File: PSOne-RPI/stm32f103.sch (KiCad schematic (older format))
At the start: 13 parts, among them J10 Controller-Port, J11 Controller-Port, SW1 PWR_BTN, SW2 CD_CLOSED, U7 STM32F103RBTx, Y1 8MHz

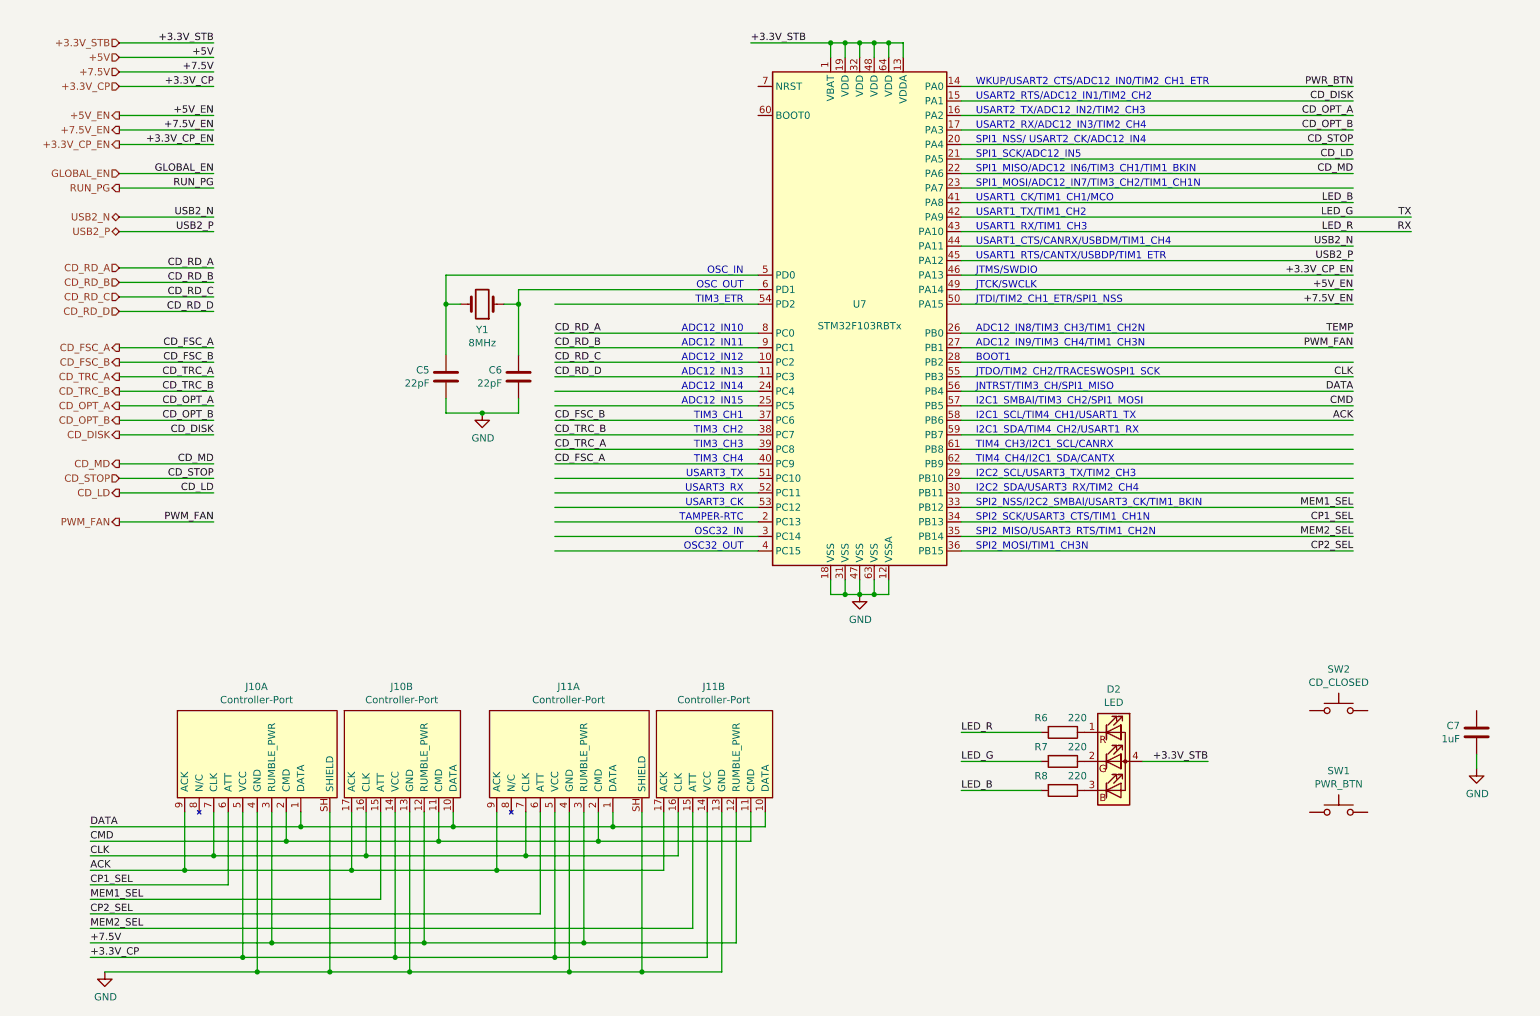
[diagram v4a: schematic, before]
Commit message: Added possibility to use the STM32 as RTC
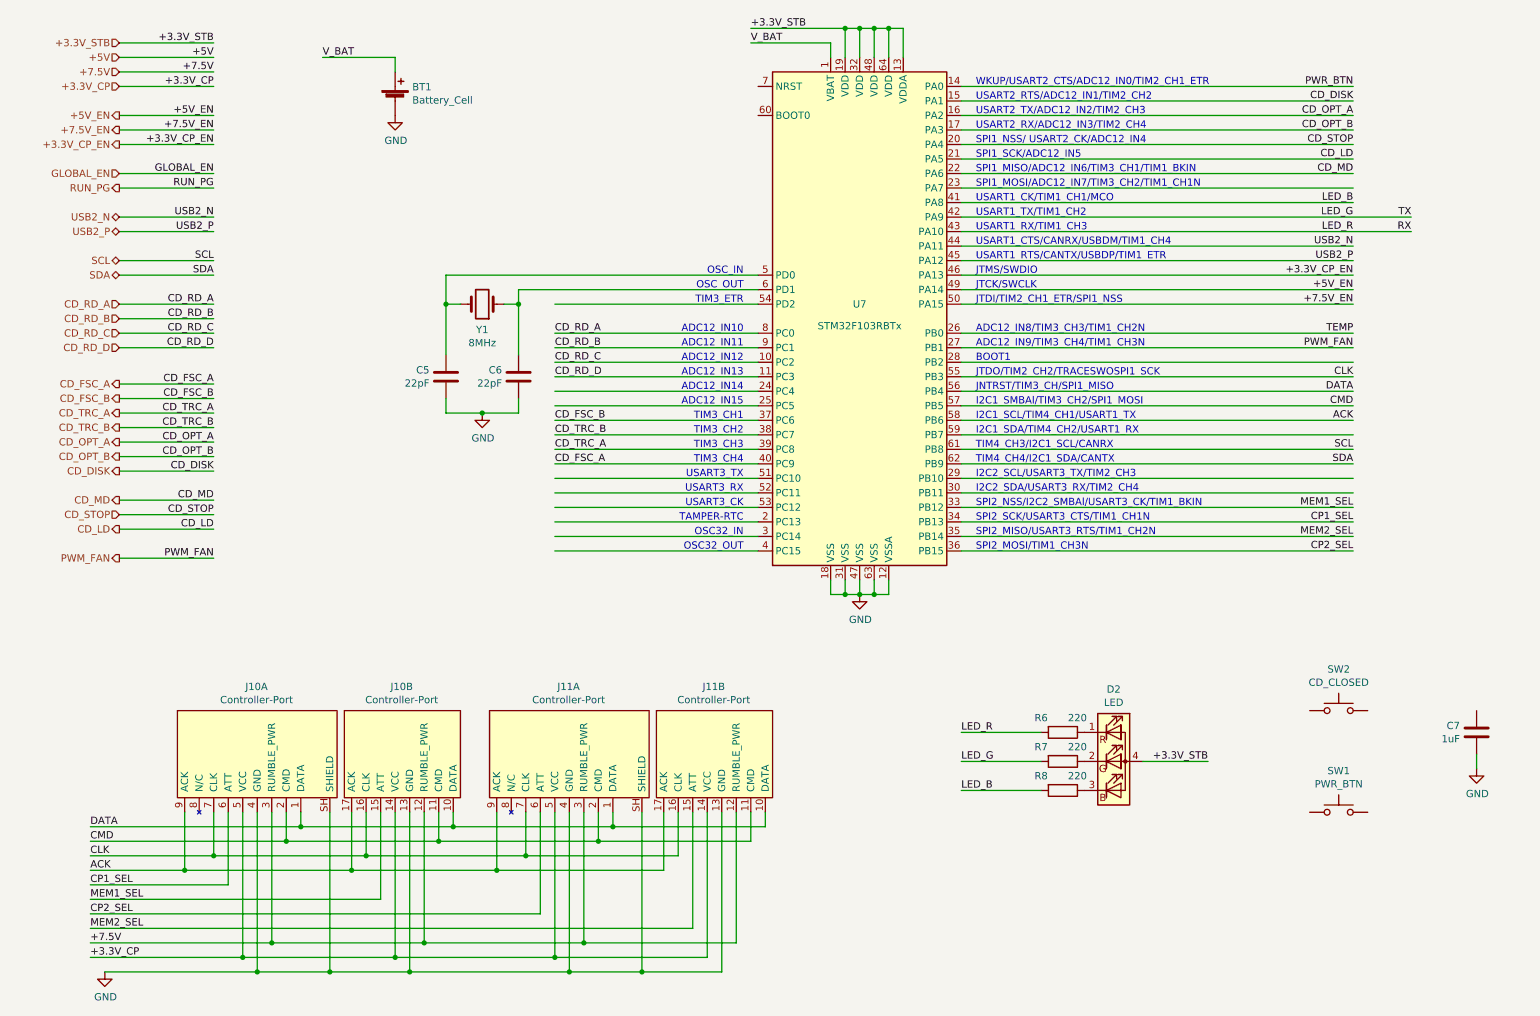
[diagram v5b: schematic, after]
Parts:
- added BT1: Battery_Cell, Battery:BatteryHolder_Keystone_1058_1x2032, symbol Device:Battery_Cell
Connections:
- net labels added: SCL, SDA, V_BAT
- wire segments 181 -> 185
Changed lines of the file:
@@
 Text Label 1200 6250 0    50   ~ 0
 DATA
-Wire Wire Line
-	6300 850  6400 850
-Wire Wire Line
-	6700 850  6700 950
-Wire Wire Line
-	6300 850  6300 950
-Wire Wire Line
-	6600 950  6600 850
-Connection ~ 6600 850
-Wire Wire Line
-	6600 850  6700 850
-Wire Wire Line
-	6500 950  6500 850
-Connection ~ 6500 850
-Wire Wire Line
-	6500 850  6600 850
-Wire Wire Line
-	6400 950  6400 850
-Connection ~ 6400 850
-Wire Wire Line
-	6400 850  6500 850
-Connection ~ 6300 850
-Text Label 5750 850  0    50   ~ 0
+Connection ~ 6600 750
+Wire Wire Line
+	6600 750  6700 750
+Connection ~ 6500 750
+Wire Wire Line
+	6500 750  6600 750
+Connection ~ 6400 750
+Wire Wire Line
+	6400 750  6500 750
+Text Label 5750 750  0    50   ~ 0
 +3.3V_STB
 Text Label 9900 3450 2    50   ~ 0
@@
 $EndComp
 Wire Wire Line
-	6700 850  6800 850
-Wire Wire Line
-	6800 850  6800 950
-Connection ~ 6700 850
+	6700 750  6800 750
+Connection ~ 6700 750
 Wire Wire Line
 	6600 4650 6700 4650
@@
 Text Label 9900 2650 2    50   ~ 0
 +7.5V_EN
-Wire Wire Line
-	5750 850  6300 850
 Text Label 9900 2450 2    50   ~ 0
 +3.3V_CP_EN
@@
 Text Label 2050 1150 2    50   ~ 0
 +3.3V_CP
-Text HLabel 1400 2400 0    50   Input ~ 0
+Text HLabel 1400 2650 0    50   Input ~ 0
 CD_RD_A
-Text HLabel 1400 2500 0    50   Input ~ 0
+Text HLabel 1400 2750 0    50   Input ~ 0
 CD_RD_B
-Text HLabel 1400 2600 0    50   Input ~ 0
+Text HLabel 1400 2850 0    50   Input ~ 0
 CD_RD_C
-Text HLabel 1400 2700 0    50   Input ~ 0
+Text HLabel 1400 2950 0    50   Input ~ 0
 CD_RD_D
 Wire Wire Line
-	1400 2400 2050 2400
-Wire Wire Line
-	1400 2500 2050 2500
-Wire Wire Line
-	1400 2600 2050 2600
-Wire Wire Line
-	1400 2700 2050 2700
-Text Label 2050 2400 2    50   ~ 0
+	1400 2650 2050 2650
+Wire Wire Line
+	1400 2750 2050 2750
+Wire Wire Line
+	1400 2850 2050 2850
+Wire Wire Line
+	1400 2950 2050 2950
+Text Label 2050 2650 2    50   ~ 0
 CD_RD_A
-Text Label 2050 2500 2    50   ~ 0
+Text Label 2050 2750 2    50   ~ 0
 CD_RD_B
-Text Label 2050 2600 2    50   ~ 0
+Text Label 2050 2850 2    50   ~ 0
 CD_RD_C
-Text Label 2050 2700 2    50   ~ 0
+Text Label 2050 2950 2    50   ~ 0
 CD_RD_D
-Text HLabel 1400 2950 0    50   Output ~ 0
+Text HLabel 1400 3200 0    50   Output ~ 0
 CD_FSC_A
-Text HLabel 1400 3050 0    50   Output ~ 0
+Text HLabel 1400 3300 0    50   Output ~ 0
 CD_FSC_B
-Text HLabel 1400 3150 0    50   Output ~ 0
+Text HLabel 1400 3400 0    50   Output ~ 0
 CD_TRC_A
-Text HLabel 1400 3250 0    50   Output ~ 0
+Text HLabel 1400 3500 0    50   Output ~ 0
 CD_TRC_B
 Wire Wire Line
-	1400 2950 2050 2950
-Wire Wire Line
-	1400 3050 2050 3050
-Text Label 2050 2950 2    50   ~ 0
+	1400 3200 2050 3200
+Wire Wire Line
+	1400 3300 2050 3300
+Text Label 2050 3200 2    50   ~ 0
 CD_FSC_A
-Text Label 2050 3050 2    50   ~ 0
+Text Label 2050 3300 2    50   ~ 0
 CD_FSC_B
 Wire Wire Line
-	1400 3150 2050 3150
-Wire Wire Line
-	1400 3250 2050 3250
-Text Label 2050 3150 2    50   ~ 0
+	1400 3400 2050 3400
+Wire Wire Line
+	1400 3500 2050 3500
+Text Label 2050 3400 2    50   ~ 0
 CD_TRC_A
-Text Label 2050 3250 2    50   ~ 0
+Text Label 2050 3500 2    50   ~ 0
 CD_TRC_B
-Text HLabel 1400 3350 0    50   Output ~ 0
+Text HLabel 1400 3600 0    50   Output ~ 0
 CD_OPT_A
-Text HLabel 1400 3450 0    50   Output ~ 0
+Text HLabel 1400 3700 0    50   Output ~ 0
 CD_OPT_B
 Wire Wire Line
-	1400 3350 2050 3350
-Wire Wire Line
-	1400 3450 2050 3450
-Text Label 2050 3350 2    50   ~ 0
+	1400 3600 2050 3600
+Wire Wire Line
+	1400 3700 2050 3700
+Text Label 2050 3600 2    50   ~ 0
 CD_OPT_A
-Text Label 2050 3450 2    50   ~ 0
+Text Label 2050 3700 2    50   ~ 0
 CD_OPT_B
-Text HLabel 1400 3550 0    50   Output ~ 0
+Text HLabel 1400 3800 0    50   Output ~ 0
 CD_DISK
 Wire Wire Line
-	1400 3550 2050 3550
-Text Label 2050 3550 2    50   ~ 0
+	1400 3800 2050 3800
+Text Label 2050 3800 2    50   ~ 0
 CD_DISK
-Text HLabel 1400 4150 0    50   Output ~ 0
+Text HLabel 1400 4400 0    50   Output ~ 0
 PWM_FAN
 Wire Wire Line
-	1400 4150 2050 4150
-Text Label 2050 4150 2    50   ~ 0
+	1400 4400 2050 4400
+Text Label 2050 4400 2    50   ~ 0
 PWM_FAN
 Wire Wire Line
@@
 Wire Wire Line
 	8450 5800 8900 5800
-Text HLabel 1400 3750 0    50   Output ~ 0
+Text HLabel 1400 4000 0    50   Output ~ 0
 CD_MD
 Wire Wire Line
-	1400 3750 2050 3750
-Text Label 2050 3750 2    50   ~ 0
+	1400 4000 2050 4000
+Text Label 2050 4000 2    50   ~ 0
 CD_MD
 Text Label 9900 1750 2    50   ~ 0
 CD_MD
-Text HLabel 1400 3850 0    50   Input ~ 0
+Text HLabel 1400 4100 0    50   Input ~ 0
 CD_STOP
 Wire Wire Line
-	1400 3850 2050 3850
-Text Label 2050 3850 2    50   ~ 0
+	1400 4100 2050 4100
+Text Label 2050 4100 2    50   ~ 0
 CD_STOP
-Text HLabel 1400 3950 0    50   Output ~ 0
+Text HLabel 1400 4200 0    50   Output ~ 0
 CD_LD
 Wire Wire Line
-	1400 3950 2050 3950
-Text Label 2050 3950 2    50   ~ 0
+	1400 4200 2050 4200
+Text Label 2050 4200 2    50   ~ 0
 CD_LD
 Text Label 9900 1550 2    50   ~ 0
@@
 Wire Wire Line
 	7200 4350 9900 4350
+$Comp
+L Device:Battery_Cell BT1
+U 1 1 5FEF6B17
+P 3300 1250
+F 0 "BT1" H 3418 1346 50  0000 L CNN
+F 1 "Battery_Cell" H 3418 1255 50  0000 L CNN
+F 2 "Battery:BatteryHolder_Keystone_1058_1x2032" V 3300 1310 50  0001 C CNN
+F 3 "~" V 3300 1310 50  0001 C CNN
+	1    3300 1250
+	1    0    0    -1
+$EndComp
+$Comp
+L power:GND #PWR0142
+U 1 1 5FEF7071
+P 3300 1350
+F 0 "#PWR0142" H 3300 1100 50  0001 C CNN
+F 1 "GND" H 3305 1177 50  0000 C CNN
+F 2 "" H 3300 1350 50  0001 C CNN
+F 3 "" H 3300 1350 50  0001 C CNN
+	1    3300 1350
+	1    0    0    -1
+$EndComp
+Wire Wire Line
+	3300 1050 3300 950
+Wire Wire Line
+	3300 950  2800 950
+Text Label 2800 950  0    50   ~ 0
+V_BAT
+Wire Wire Line
+	5750 750  6400 750
+Wire Wire Line
+	6400 750  6400 950
+Wire Wire Line
+	6500 750  6500 950
+Wire Wire Line
+	6600 750  6600 950
+Wire Wire Line
+	6700 750  6700 950
+Wire Wire Line
+	6800 750  6800 950
+Wire Wire Line
+	6300 950  6300 850
+Wire Wire Line
+	6300 850  5750 850
+Text Label 5750 850  0    50   ~ 0
+V_BAT
+Text Label 9900 3650 2    50   ~ 0
+SCL
+Text Label 9900 3750 2    50   ~ 0
+SDA
+Text HLabel 1400 2450 0    50   BiDi ~ 0
+SDA
+Text HLabel 1400 2350 0    50   BiDi ~ 0
+SCL
+Wire Wire Line
+	1400 2350 2050 2350
+Wire Wire Line
+	1400 2450 2050 2450
+Text Label 2050 2350 2    50   ~ 0
+SCL
+Text Label 2050 2450 2    50   ~ 0
+SDA
 $EndSCHEMATC
